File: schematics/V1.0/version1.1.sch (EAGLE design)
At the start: 94 parts, among them IC1 ADG1604S, IC2 LM317MBSTT3, IC3 AD8610MR, IC4 AD8610MR, IC5 337IMP, Q1 16MHz, T1 BC847, T2 BC847, T3 BC847, T4 BC847, X2 BU-SMA-H

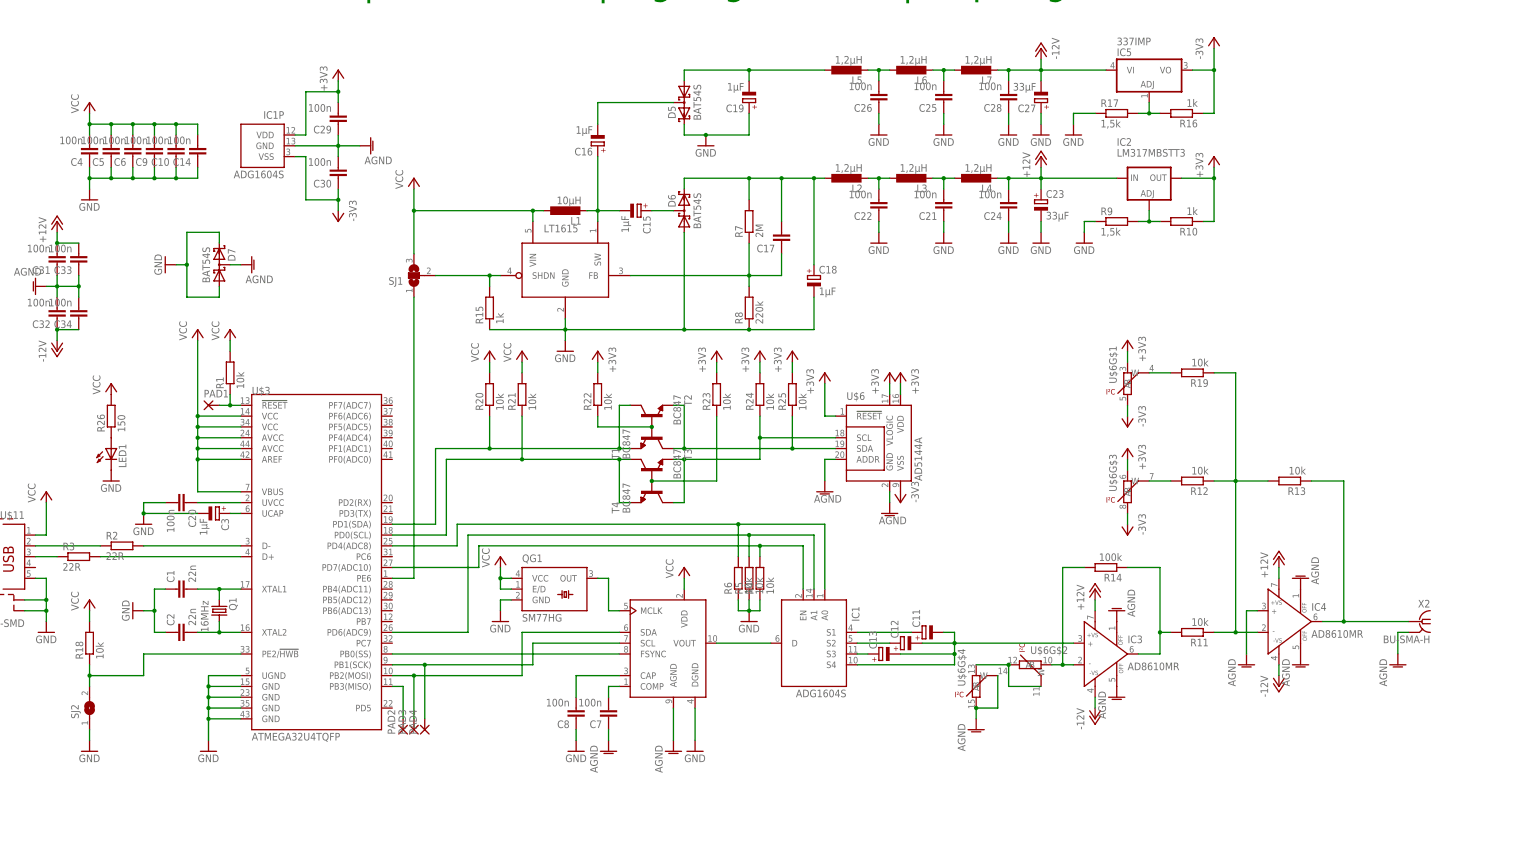
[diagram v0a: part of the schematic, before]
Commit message: change the circuit diagramm because of amplification-issues
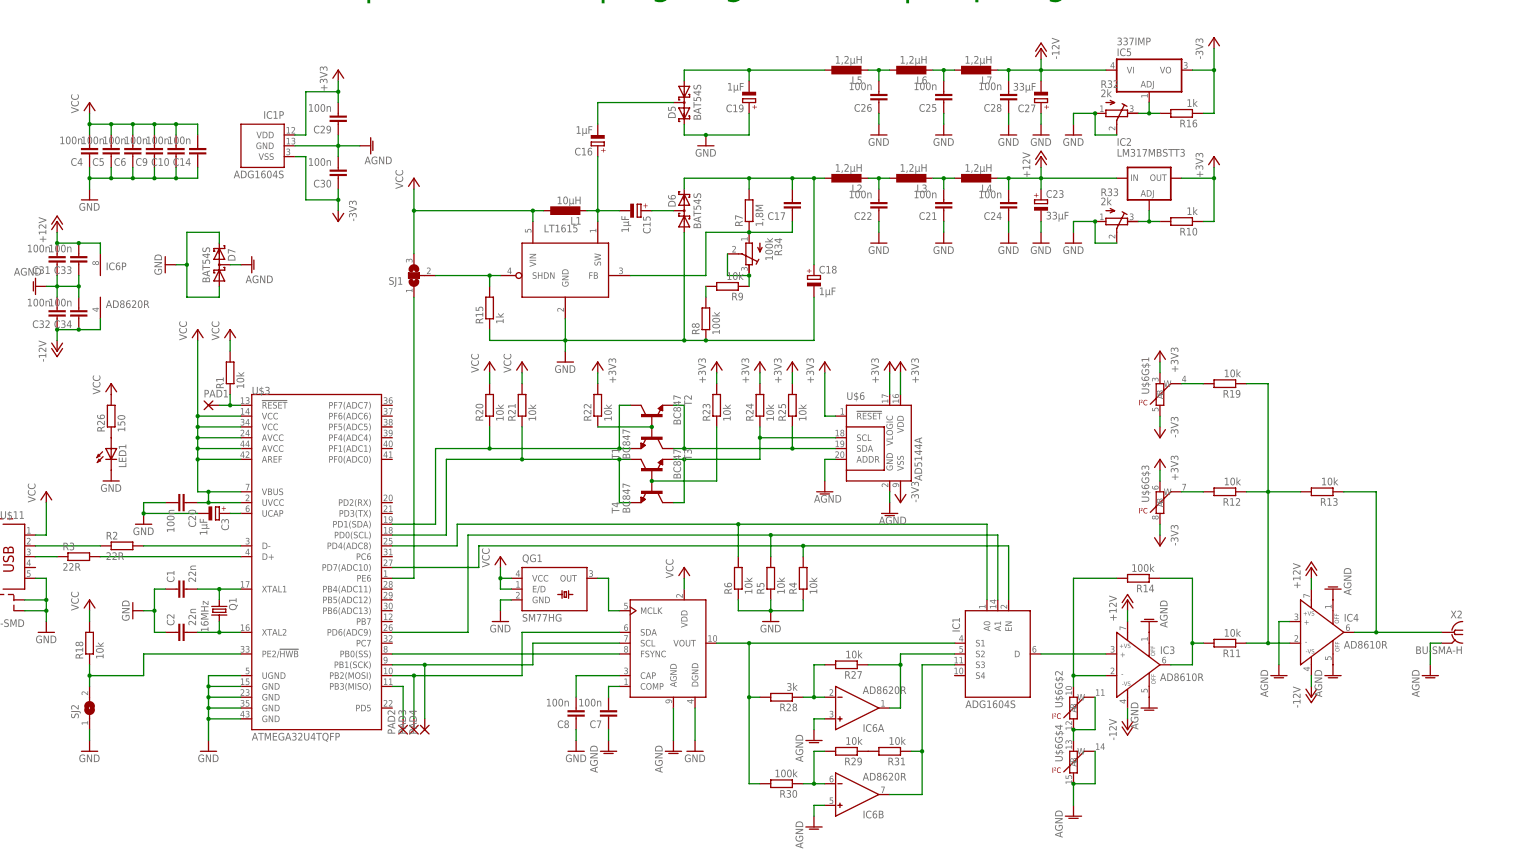
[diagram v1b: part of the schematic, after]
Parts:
- removed C11, C12, C13: (no value), rcl:CPOL-EUSMCB
- removed R17: 1,5k, rcl:R-EU_R0603
- added IC6: AD8620R, analog-devices:AD8620R
- added R27, R29, R31: 10k, rcl:R-EU_R0603
- added R28: 3k, rcl:R-EU_R0603
- added R30: 100k, rcl:R-EU_R0603
- added R32, R33: 2k, rcl:R-TRIMM3224W
- added R34: 100k, rcl:R-TRIMM3224W
- IC3, IC4: value AD8610MR -> AD8610R; device analog-devices:AD8610MR -> analog-devices:AD8610R
- R7: value 2M -> 1,8M
- R8: value 220k -> 100k
- R9: value 1,5k -> 10k
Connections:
- new net N$54: R29.1, R31.2
- new net N$55: C17.1, R34.A, R7.1, U$2.FB
- new net N$57: R34.E, R34.S, R9.1
- net +12V: now also IC6P.V+
- net -12V: now also IC6P.V-
- net AGND: now also IC6A.IN+, IC6B.IN+
- net GND: now also R32.A, R32.S, R33.A, R33.S; no longer R17.1, R9.1
- net N$16: now also IC1G$1.S1, R28.2, R30.2; no longer IC1G$1.D
- net N$17: now also IC6A.IN-, R27.2, R28.1; no longer C13.+, IC1G$1.S3
- net N$18: now also IC6A.OUT, R27.1; no longer C12.+
- net N$19: now also IC1G$1.S3, IC6B.OUT, R31.1; no longer C11.+, IC1G$1.S1
- net N$20: now also IC1G$1.D; no longer C11.-, C12.-, C13.-, IC1G$1.S4
- net N$27: now also R9.2; no longer C17.1, R7.1, U$2.FB
- net N$30: now also R33.E; no longer R9.2
- net N$41: now also R32.E; no longer R17.2
- net N$53: now also IC6B.IN-, R29.2, R30.1; no longer C20.1, U$3.UVCC
- net VCC: now also C20.1, U$3.UVCC
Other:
- moved on the sheet: C17, IC1, IC3, IC4, R11, R12, R13, R14, R19, R20, R21, R22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
